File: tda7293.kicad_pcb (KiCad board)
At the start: 2 copper layers, 100 x 48 mm, 60 parts, among them J1 Screw_Terminal_01x04, J2 Screw_Terminal_01x04, J3 Screw_Terminal_01x02, J4 Screw_Terminal_01x03, Q1 BSS84, Q2 2N7002, U1 TDA7293, U2 TDA7293, U3 PC817, U4 MCP1792

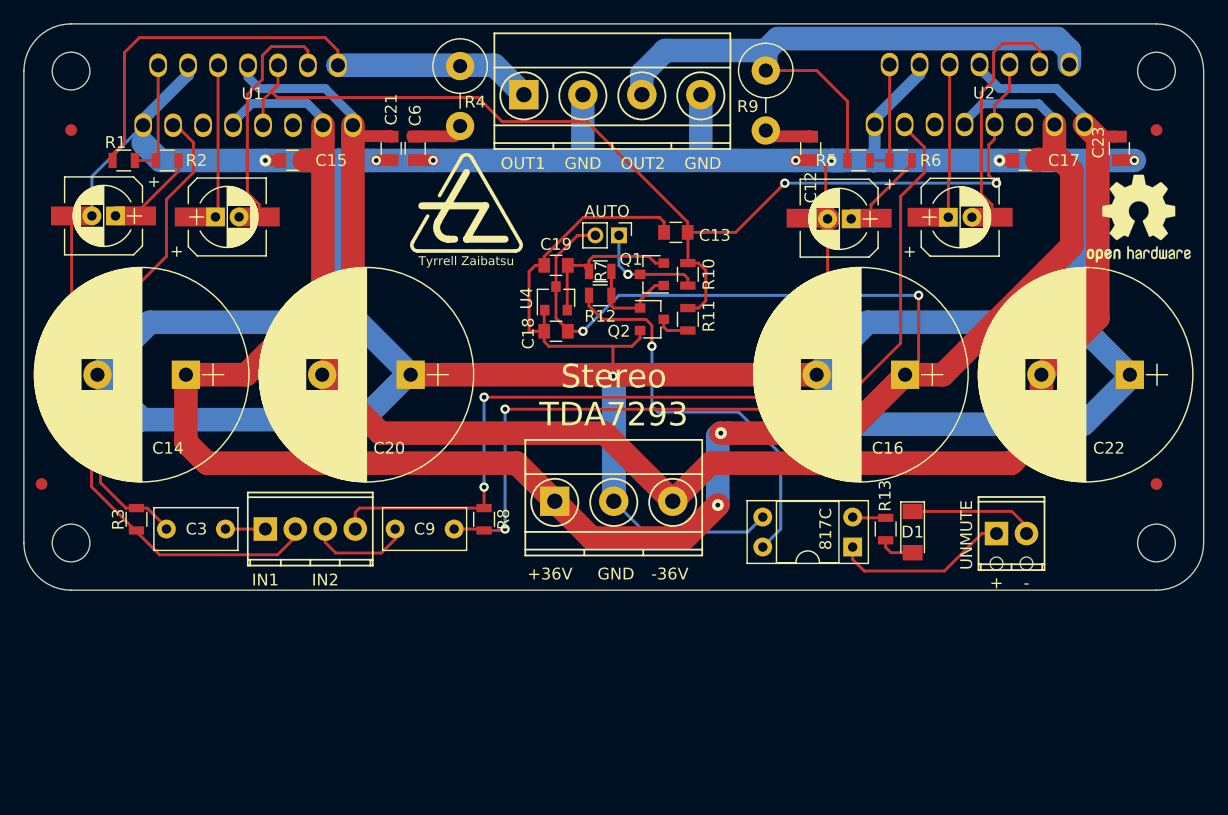
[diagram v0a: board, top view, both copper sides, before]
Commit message: layout turd-polishing, renamed to TDA7293 due to removal of bootstrap jumper
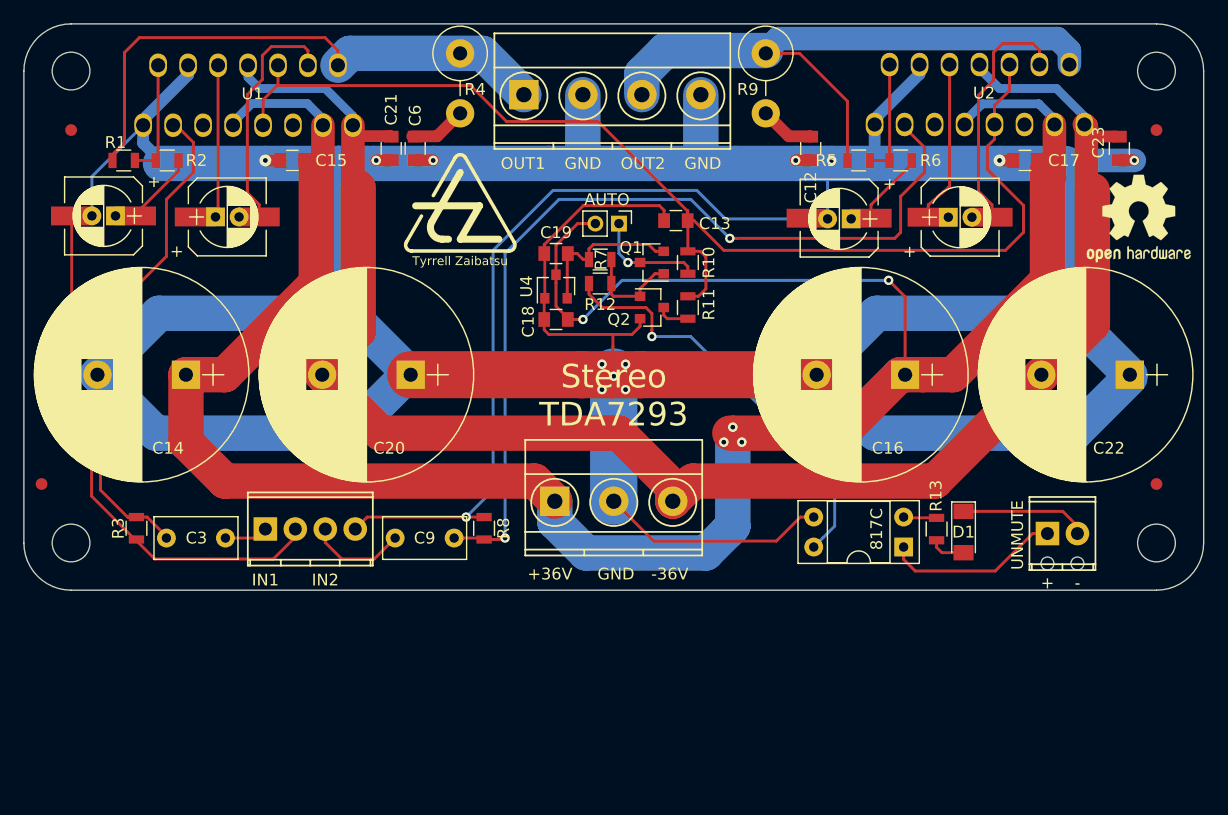
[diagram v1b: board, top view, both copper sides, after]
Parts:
- moved J3 4.32 mm to (111.8, 68.2)
- moved D1 4.32 mm to (104.6, 68.1)
- moved R13 4.32 mm to (102.4, 67.8)
- moved U3 4.32 mm to (99.6, 69.3)
- moved R9 1.46 mm to (87.9, 27.5)
- moved R4 1.07 mm to (62.0, 27.5)
- moved C13 1.00 mm to (80.3, 41.7)
- moved C18 1.00 mm to (70.1, 50.1)
- moved C19 1.00 mm to (70.1, 44.5)
- moved JP3 1.00 mm to (75.4, 41.9)
- moved Q1 1.00 mm to (78.2, 45.2)
- moved Q2 1.00 mm to (78.2, 49.0)
- moved R10 1.00 mm to (81.3, 45.2)
- moved R11 1.00 mm to (81.3, 49.0)
- moved R12 1.00 mm to (73.8, 47.0)
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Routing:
- net /GND: track 506.2 -> 497.9 mm, vias 10 -> 13
- net /MUTE: track 94.8 -> 101.8 mm, vias 2 -> 0
- net Net-(C9-Pad1): track 70.5 -> 76.2 mm
- net /VEE: track 149.6 -> 146.5 mm
- net /VCC: track 209.5 -> 212.1 mm, vias 4 -> 5
- net /OUT2: track 55.6 -> 54.5 mm
- net Net-(R12-Pad1): track 34.9 -> 35.8 mm
- net /OUT1: track 46.7 -> 47.5 mm
- net Net-(C10-Pad1): track 13.0 -> 13.8 mm
- net /5V: track 14.2 -> 13.5 mm
- net Net-(C3-Pad1): track 44.7 -> 45.4 mm
- net Net-(C12-Pad1): track 4.03 -> 4.63 mm
- net Net-(C6-Pad1): track 4.27 -> 4.87 mm

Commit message: C substitutions, status LEDs, layout polishing
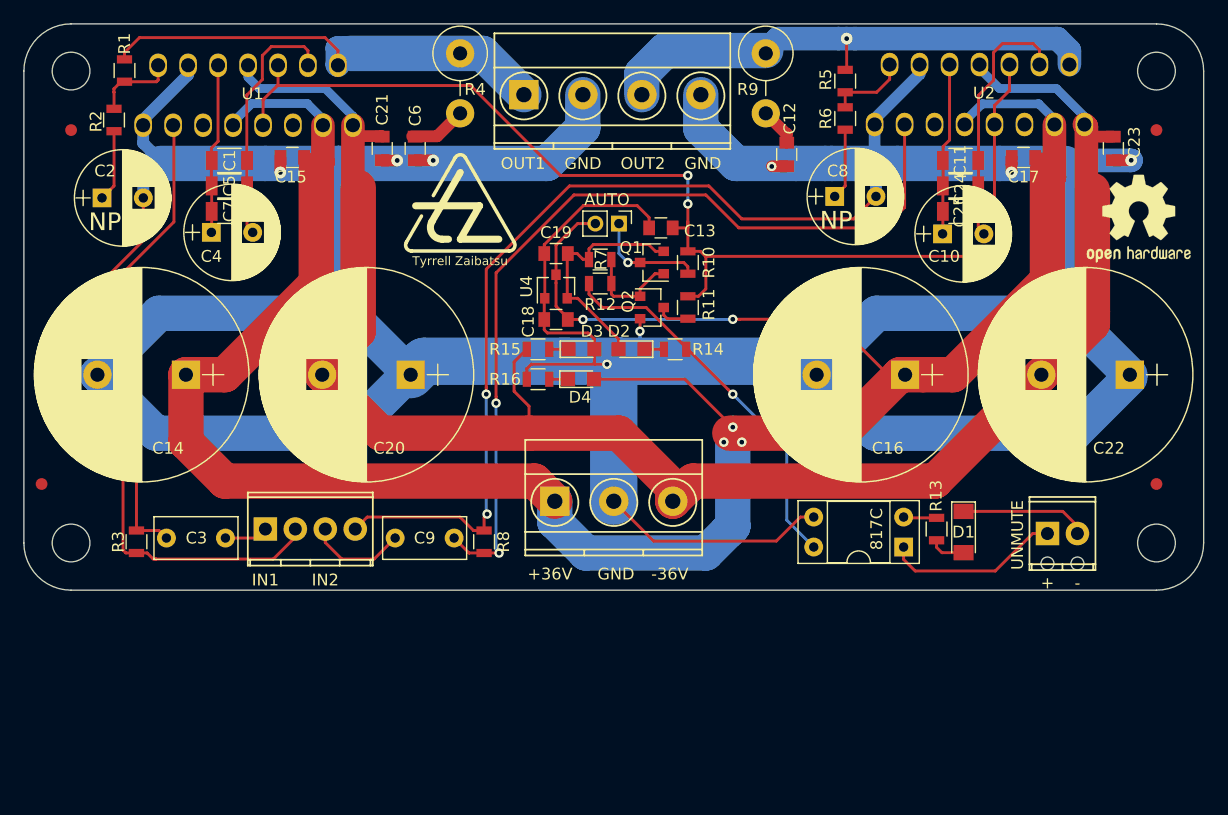
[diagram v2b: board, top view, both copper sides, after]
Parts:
- added C24: 10u, Capacitors_SMD:C_1206, F.Cu at (104.4, 38.7)
- added C25: 10u, Capacitors_SMD:C_1206, F.Cu at (104.4, 40.9)
- added D2: LED, LEDs:LED_0805, F.Cu at (76.5, 52.6)
- added D3: LED, LEDs:LED_0805, F.Cu at (72.3, 52.6)
- added D4: LED, LEDs:LED_0805, F.Cu at (72.2, 55.1)
- added R14: 1k, Resistors_SMD:R_0805, F.Cu at (80.2, 52.6)
- added R15: 10k, Resistors_SMD:R_0805, F.Cu at (68.6, 52.6)
- added R16: 10k, Resistors_SMD:R_0805, F.Cu at (68.6, 55.1)
- C1, C7: value 22u -> 10u; footprint Capacitors_SMD:CP_Elec_6.3x7.7 -> Capacitors_SMD:C_1206
- C10, C4: footprint Capacitors_SMD:CP_Elec_6.3x7.7 -> Capacitors_ThroughHole:CP_Radial_D8.0mm_P3.50mm
- C11, C5: value 22u -> 10u; footprint Capacitors_ThroughHole:CP_Radial_D5.0mm_P2.00mm -> Capacitors_SMD:C_1206
- C2, C8: value 22u -> 22u NP; footprint Capacitors_ThroughHole:CP_Radial_D5.0mm_P2.00mm -> Capacitors_ThroughHole:CP_Radial_D8.0mm_P3.50mm
- moved C7 51.7 mm to (42.4, 40.9)
- moved C1 11.7 mm to (42.4, 36.6)
- moved R1 7.62 mm to (33.5, 29.0), turned to 90 degrees
- moved R5 6.83 mm to (94.6, 29.8), turned to 90 degrees
- moved R6 5.89 mm to (94.6, 33.0), turned to 270 degrees
- moved R2 5.67 mm to (32.6, 33.1), turned to 270 degrees
- moved C11 4.92 mm to (104.4, 36.6), turned to 180 degrees
- moved C5 2.88 mm to (42.4, 38.7), turned to 180 degrees
- moved C8 2.36 mm to (93.7, 39.6), turned to 0 degrees
- moved C12 2.09 mm to (89.7, 36.1)
- moved C10 2.05 mm to (102.9, 42.8)
- moved C2 1.90 mm to (31.6, 39.8), turned to 0 degrees
- moved C4 1.88 mm to (40.9, 42.7)
- moved C13 1.41 mm to (79.0, 42.3)
- moved R3 1.14 mm to (34.5, 68.9)
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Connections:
- C1 pad 2: /GND -> Net-(C1-Pad2)
- C11 pad 1: Net-(C10-Pad1) -> Net-(C10-Pad2)
- C11 pad 2: Net-(C10-Pad2) -> Net-(C10-Pad1)
- C2 pad 1: Net-(C1-Pad1) -> Net-(C2-Pad1)
- C4 pad 1: Net-(C4-Pad1) -> Net-(C1-Pad2)
- C4 pad 2: Net-(C4-Pad2) -> Net-(C1-Pad1)
- C5 pad 1: Net-(C4-Pad1) -> Net-(C1-Pad1)
- C5 pad 2: Net-(C4-Pad2) -> Net-(C1-Pad2)
- C7 pad 1: Net-(C7-Pad1) -> Net-(C1-Pad1)
- C7 pad 2: /GND -> Net-(C1-Pad2)
- C8 pad 1: Net-(C7-Pad1) -> Net-(C8-Pad1)
- R2 pad 2: Net-(C1-Pad1) -> Net-(C2-Pad1)
- R6 pad 2: Net-(C7-Pad1) -> Net-(C8-Pad1)
- U1 pad 12: Net-(C4-Pad2) -> Net-(C1-Pad1)
- U1 pad 6: Net-(C4-Pad1) -> Net-(C1-Pad2)
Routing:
- net Net-(C4-Pad2): track 20.2 -> 0.00 mm
- net Net-(C1-Pad1): track 5.81 -> 21.3 mm
- net Net-(C1-Pad2): track 0.00 -> 14.4 mm
- net Net-(C4-Pad1): track 13.6 -> 0.00 mm
- net /OUT2: track 54.5 -> 43.6 mm, vias 0 -> 1
- net Net-(C7-Pad1): track 8.03 -> 0.00 mm
- net /OUT1: track 47.5 -> 39.8 mm
- net /VEE: track 146.5 -> 154.1 mm
- net /5V: track 13.5 -> 20.2 mm
- net Net-(C2-Pad1): track 0.00 -> 6.07 mm
- net Net-(C8-Pad1): track 0.00 -> 6.02 mm
- net /VCC: track 212.1 -> 217.7 mm
- net /GND: track 497.9 -> 494.3 mm, vias 13 -> 10
- net Net-(R1-Pad1): track 10.2 -> 7.01 mm
- net Net-(R12-Pad1): track 35.8 -> 32.8 mm
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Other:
- board text added: "NP"
- board text added: "short for TDA7294"
- board text removed: "Stereo TDA7293"

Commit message: polishing, plotted output, added README
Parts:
- removed JP3: Jumper_NO_Small, Pin_Headers:Pin_Header_Straight_1x02_Pitch2.00mm
- added R17: 47k, Resistors_SMD:R_0805, F.Cu at (47.8, 38.4)
- added R18: 47k, Resistors_SMD:R_0805, F.Cu at (55.4, 38.6)
- moved REF** 3.83 mm to (75.0, 49.0)
- moved C12 3.31 mm to (91.4, 33.3)
- moved C6 2.30 mm to (58.4, 33.3)
- moved R1 1.02 mm to (33.5, 30.0)
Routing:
- net /VCC: track 217.7 -> 212.0 mm
- net /GND: track 494.3 -> 499.7 mm
- net Net-(Q1-Pad3): track 9.44 -> 4.79 mm, vias 1 -> 0
- net Net-(R1-Pad1): track 7.01 -> 5.50 mm
- net Net-(R12-Pad1): track 32.8 -> 34.2 mm
- net /MUTE: track 100.1 -> 98.9 mm
- net Net-(C6-Pad1): track 4.87 -> 3.68 mm
- net /OUT1: track 39.8 -> 40.8 mm
- net Net-(C9-Pad1): track 74.5 -> 73.5 mm
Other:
- board text removed: "AUTO"

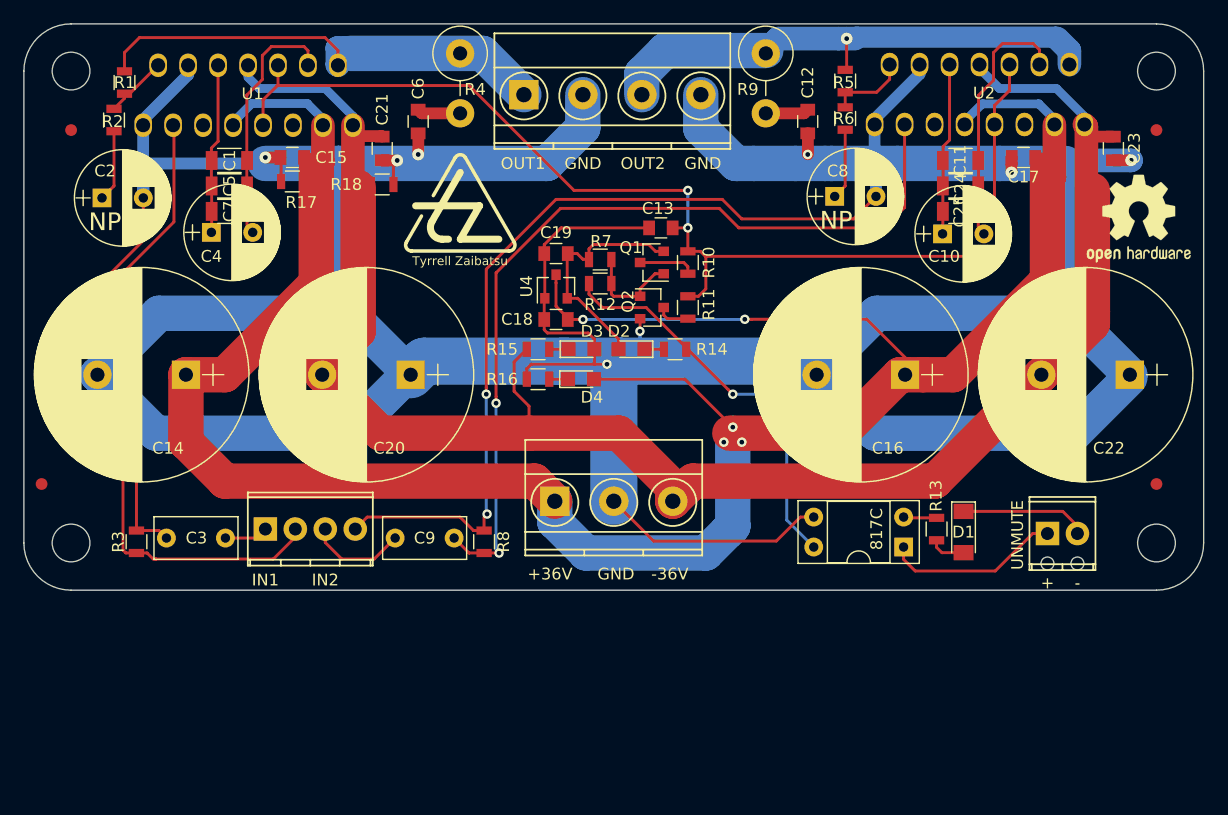
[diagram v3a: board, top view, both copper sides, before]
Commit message: removed holes, moved input filters, fancier unmute timing per datasheet
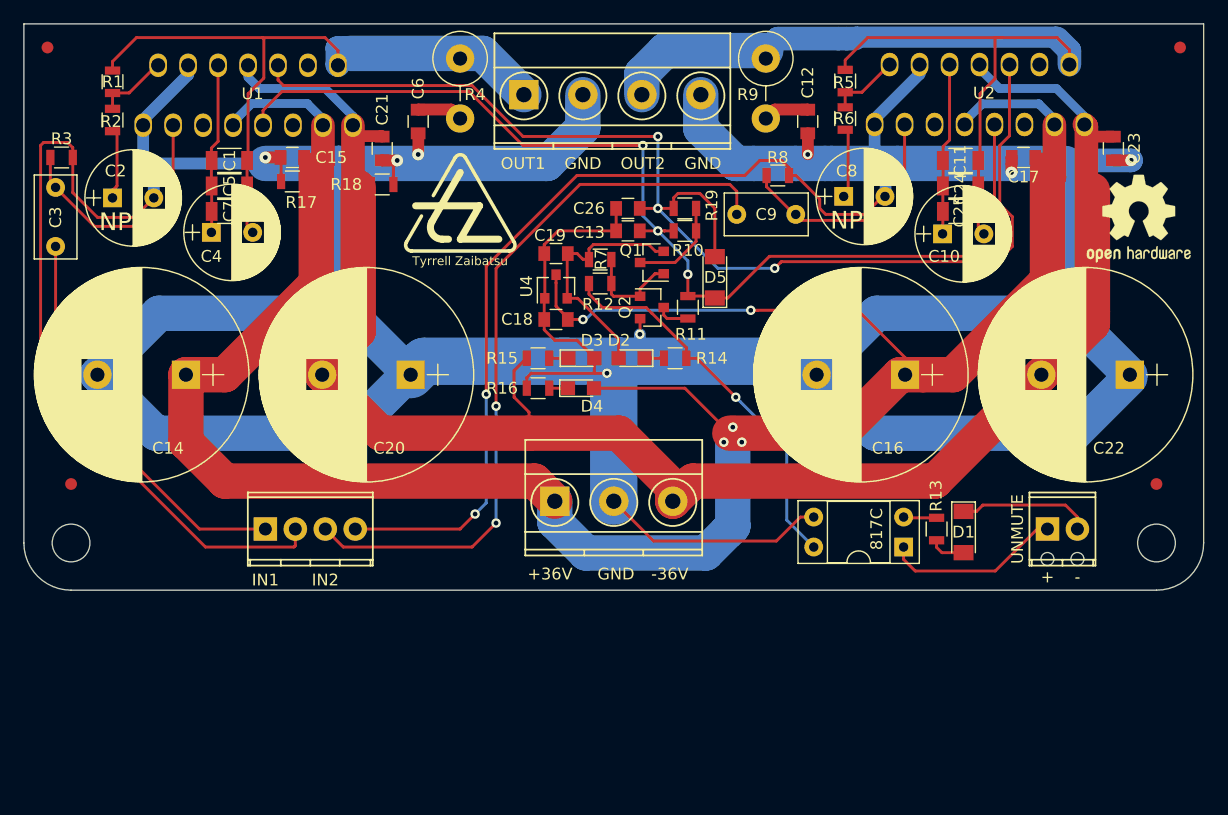
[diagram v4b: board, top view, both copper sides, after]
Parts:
- removed H3, H4: MountingHole, Mounting_Holes:MountingHole_3.2mm_M3
- added C26: 10u, Capacitors_SMD:C_0805, F.Cu at (76.2, 40.6)
- added D5: LL4148, Diodes_SMD:D_MiniMELF, F.Cu at (83.6, 46.5)
- added R19: 27k, Resistors_SMD:R_0805, F.Cu at (81.0, 40.6)
- R17, R18: value 47k -> 27k
- moved H1 40.0 mm to (29.0, 69.0)
- moved H2 40.0 mm to (121.0, 69.0)
- moved C9 39.9 mm to (90.4, 41.1)
- moved R8 39.8 mm to (88.9, 37.8), turned to 180 degrees
- moved R3 33.2 mm to (28.2, 36.3), turned to 180 degrees
- moved C3 31.2 mm to (27.7, 38.9), turned to 270 degrees
- moved FID2 7.28 mm to (27.0, 27.0)
- moved FID3 7.28 mm to (123.0, 27.0)
- moved C13 2.81 mm to (76.2, 42.5)
- moved R10 2.69 mm to (81.0, 42.5), turned to 180 degrees
- moved FID4 2.50 mm to (29.0, 64.0)
- moved R1 1.02 mm to (32.5, 29.9)
- moved C2 0.89 mm to (32.5, 39.8)
- moved C8 0.76 mm to (94.5, 39.6)
- moved D2 0.76 mm to (76.5, 53.3)
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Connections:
- C1 pad 1: Net-(C1-Pad1) -> /OUT1
- C10 pad 2: Net-(C10-Pad2) -> /OUT2
- C11 pad 1: Net-(C10-Pad2) -> /OUT2
- C13 pad 2: /MUTE -> /STBY
- C24 pad 1: Net-(C10-Pad2) -> /OUT2
- C25 pad 1: Net-(C10-Pad2) -> /OUT2
- C4 pad 2: Net-(C1-Pad1) -> /OUT1
- C5 pad 1: Net-(C1-Pad1) -> /OUT1
- C7 pad 1: Net-(C1-Pad1) -> /OUT1
- R10 pad 2: /MUTE -> /STBY
- R11 pad 1: Net-(Q2-Pad3) -> /STBY
- R11 pad 2: /MUTE -> Net-(Q2-Pad3)
- U1 pad 12: Net-(C1-Pad1) -> Net-(U1-Pad12)
- U1 pad 9: /MUTE -> /STBY
- U2 pad 12: Net-(C10-Pad2) -> Net-(U2-Pad12)
- U2 pad 9: /MUTE -> /STBY
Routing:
- net /STBY: track 0.00 -> 92.8 mm, vias 0 -> 3
- net Net-(C9-Pad2): track 8.38 -> 63.1 mm, vias 0 -> 2
- net Net-(C9-Pad1): track 73.5 -> 21.0 mm, vias 2 -> 0
- net /OUT2: track 43.7 -> 81.4 mm, vias 1 -> 0
- net Net-(C3-Pad2): track 3.70 -> 34.6 mm
- net Net-(C10-Pad2): track 21.7 -> 0.00 mm
- net Net-(C3-Pad1): track 44.2 -> 22.8 mm
- net Net-(C1-Pad1): track 21.3 -> 0.00 mm
- net /OUT1: track 40.8 -> 59.0 mm
- net /GND: track 499.7 -> 511.8 mm
- net /MUTE: track 98.9 -> 103.1 mm, vias 2 -> 3
- net Net-(Q1-Pad3): track 4.79 -> 8.29 mm
- net Net-(D1-Pad1): track 10.8 -> 11.7 mm
- net Net-(R12-Pad1): track 34.2 -> 33.4 mm
- net /5V: track 20.2 -> 20.9 mm
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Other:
- outline, holes or cut-outs redrawn
- board text added: "Stereo TDA7293/TDA7294 Rev.A 202111 william@brodie-tyrrell.org github.com/phenidone"
- board text removed: "Stereo TDA7293 Rev.A 202111 william@brodie-tyrrell.org github.com/phenidone"
- board text removed: "short for TDA7294"
